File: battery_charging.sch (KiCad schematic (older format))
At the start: 4 parts, among them U8 MCP73831-2-OT

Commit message: clear existing annotations from schematic
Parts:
- renumbered C13 to C?, R16 to R?, R15 to R?, U8 to U?
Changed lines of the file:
@@
 VBAT
 $Comp
-L Battery_Management:MCP73831-2-OT U8
+L Battery_Management:MCP73831-2-OT U?
 U 1 1 5C91A071
 P 3200 2000
-F 0 "U8" H 3200 2481 50  0000 C CNN
+F 0 "U?" H 3200 2481 50  0000 C CNN
 F 1 "MCP73831-2-OT" H 3200 2390 50  0000 C CNN
 F 2 "Package_TO_SOT_SMD:SOT-23-5" H 3250 1750 50  0001 L CIN
@@
 	3600 2100 4000 2100
 $Comp
-L Device:R_Small_US R16
+L Device:R_Small_US R?
 U 1 1 5C91CC9C
 P 4000 1900
-F 0 "R16" H 4068 1946 50  0000 L CNN
+F 0 "R?" H 4068 1946 50  0000 L CNN
 F 1 "10k" H 4068 1855 50  0000 L CNN
 F 2 "Resistor_SMD:R_0603_1608Metric_Pad1.05x0.95mm_HandSolder" H 4000 1900 50  0001 C CNN
@@
 Connection ~ 3200 1650
 $Comp
-L Device:R_Small_US R15
+L Device:R_Small_US R?
 U 1 1 5C91D6DA
 P 2750 2300
-F 0 "R15" H 2818 2346 50  0000 L CNN
+F 0 "R?" H 2818 2346 50  0000 L CNN
 F 1 "2k" H 2818 2255 50  0000 L CNN
 F 2 "Resistor_SMD:R_0603_1608Metric_Pad1.05x0.95mm_HandSolder" H 2750 2300 50  0001 C CNN
@@
 	3200 2500 3200 2300
 $Comp
-L Device:C_Small C13
+L Device:C_Small C?
 U 1 1 5C91EAAB
 P 2600 1900
-F 0 "C13" H 2692 1946 50  0000 L CNN
+F 0 "C?" H 2692 1946 50  0000 L CNN
 F 1 "10uF" H 2692 1855 50  0000 L CNN
 F 2 "Capacitor_SMD:C_0603_1608Metric_Pad1.05x0.95mm_HandSolder" H 2600 1900 50  0001 C CNN

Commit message: fix battery status line to be pulled up to 2.8v, not +vbat
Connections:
- net labels added: VDDIO
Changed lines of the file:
@@
 	4000 2100 4100 2100
 Wire Wire Line
-	4000 1800 4000 1650
-Wire Wire Line
-	4000 1650 3200 1650
-Connection ~ 3200 1650
+	4000 1800 4000 1700
 $Comp
 L Device:R_Small_US R?
@@
 	2600 2500 2750 2500
 Connection ~ 2750 2500
+Text HLabel 4100 1700 2    50   Output ~ 0
+VDDIO
+Wire Wire Line
+	4000 1700 4100 1700
 $EndSCHEMATC

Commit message: upgrade charge circuit to use tp4056, allowing the battery to charge faster without the charger throttling itself
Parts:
- removed C?: 10uF, Capacitor_SMD:C_0603_1608Metric_Pad1.05x0.95mm_HandSolder, symbol Device:C_Small
- removed R?: 10k, Resistor_SMD:R_0603_1608Metric_Pad1.05x0.95mm_HandSolder, symbol Device:R_Small_US
- removed R?: 2k, Resistor_SMD:R_0603_1608Metric_Pad1.05x0.95mm_HandSolder, symbol Device:R_Small_US
- removed U?: MCP73831-2-OT, Package_TO_SOT_SMD:SOT-23-5, symbol Battery_Management:MCP73831-2-OT
- added C?: 10uF, Capacitor_SMD:C_0603_1608Metric_Pad1.05x0.95mm_HandSolder, symbol Device:C_Small
- added R? (x2): 10k, Resistor_SMD:R_0603_1608Metric_Pad1.05x0.95mm_HandSolder, symbol Device:R_Small_US
- added R?: 1.2k, Resistor_SMD:R_0603_1608Metric_Pad1.05x0.95mm_HandSolder, symbol Device:R_Small_US
- added R?: 0.4, Resistor_SMD:R_0603_1608Metric_Pad1.05x0.95mm_HandSolder, symbol Device:R_Small_US
- added U?: TP4056, Package_SO:SOIC-8-1EP_3.9x4.9mm_P1.27mm_EP2.41x3.3mm_ThermalVias, symbol phone:TP4056
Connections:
- net labels added: ~CHRG, ~STDBY
- net labels removed: STAT
- wire segments 18 -> 31
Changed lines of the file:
@@
 Comment4 ""
 $EndDescr
-Text HLabel 4100 2100 2    50   Output ~ 0
-STAT
-Text HLabel 2500 1650 0    50   Input ~ 0
+$Comp
+L phone:TP4056 U?
+U 1 1 5D29DB22
+P 2900 1850
+F 0 "U?" H 2900 2307 39  0000 C CNN
+F 1 "TP4056" H 2900 2232 39  0000 C CNN
+F 2 "Package_SO:SOIC-8-1EP_3.9x4.9mm_P1.27mm_EP2.41x3.3mm_ThermalVias" H 2900 1850 39  0001 C CNN
+F 3 "https://datasheet.lcsc.com/szlcsc/Nanjing-Extension-Microelectronics-TP4056_C16581.pdf" H 2900 1850 39  0001 C CNN
+	1    2900 1850
+	1    0    0    -1
+$EndComp
+Text HLabel 1950 1200 1    50   Input ~ 0
 VDD
-Text HLabel 3650 1900 2    50   Output ~ 0
+Text HLabel 3400 1750 2    50   Output ~ 0
 VBAT
+Text HLabel 2900 2350 3    50   Input ~ 0
+GND
 $Comp
-L Battery_Management:MCP73831-2-OT U?
-U 1 1 5C91A071
-P 3200 2000
-F 0 "U?" H 3200 2481 50  0000 C CNN
-F 1 "MCP73831-2-OT" H 3200 2390 50  0000 C CNN
-F 2 "Package_TO_SOT_SMD:SOT-23-5" H 3250 1750 50  0001 L CIN
-F 3 "http://ww1.microchip.com/downloads/en/DeviceDoc/20001984g.pdf" H 3050 1950 50  0001 C CNN
-	1    3200 2000
+L Device:R_Small_US R?
+U 1 1 5D2A0EB0
+P 3750 1700
+F 0 "R?" H 3818 1746 50  0000 L CNN
+F 1 "10k" H 3818 1655 50  0000 L CNN
+F 2 "Resistor_SMD:R_0603_1608Metric_Pad1.05x0.95mm_HandSolder" H 3750 1700 50  0001 C CNN
+F 3 "~" H 3750 1700 50  0001 C CNN
+	1    3750 1700
+	1    0    0    -1
+$EndComp
+$Comp
+L Device:C_Small C?
+U 1 1 5D2A0EC6
+P 1950 1700
+F 0 "C?" H 2042 1746 50  0000 L CNN
+F 1 "10uF" H 2042 1655 50  0000 L CNN
+F 2 "Capacitor_SMD:C_0603_1608Metric_Pad1.05x0.95mm_HandSolder" H 1950 1700 50  0001 C CNN
+F 3 "~" H 1950 1700 50  0001 C CNN
+	1    1950 1700
 	1    0    0    -1
 $EndComp
 Wire Wire Line
-	3600 1900 3650 1900
+	2900 2350 2900 2300
 Wire Wire Line
-	3200 2600 3200 2500
-Text HLabel 3200 2600 3    50   Input ~ 0
-GND
+	2900 1550 2900 1500
 Wire Wire Line
-	3200 1700 3200 1650
+	2900 1500 2300 1500
 Wire Wire Line
-	3200 1650 2600 1650
+	1950 1600 1950 1500
 Wire Wire Line
-	3600 2100 4000 2100
+	2450 1750 2300 1750
+Wire Wire Line
+	2300 1750 2300 1500
+Connection ~ 2300 1500
+Wire Wire Line
+	2300 1500 1950 1500
 $Comp
 L Device:R_Small_US R?
-U 1 1 5C91CC9C
-P 4000 1900
-F 0 "R?" H 4068 1946 50  0000 L CNN
-F 1 "10k" H 4068 1855 50  0000 L CNN
-F 2 "Resistor_SMD:R_0603_1608Metric_Pad1.05x0.95mm_HandSolder" H 4000 1900 50  0001 C CNN
-F 3 "~" H 4000 1900 50  0001 C CNN
-	1    4000 1900
+U 1 1 5D2AB74A
+P 2400 2150
+F 0 "R?" H 2468 2196 50  0000 L CNN
+F 1 "1.2k" H 2468 2105 50  0000 L CNN
+F 2 "Resistor_SMD:R_0603_1608Metric_Pad1.05x0.95mm_HandSolder" H 2400 2150 50  0001 C CNN
+F 3 "~" H 2400 2150 50  0001 C CNN
+	1    2400 2150
 	1    0    0    -1
 $EndComp
 Wire Wire Line
-	4000 2000 4000 2100
-Connection ~ 4000 2100
+	2450 1950 2400 1950
 Wire Wire Line
-	4000 2100 4100 2100
+	2400 1950 2400 2050
 Wire Wire Line
-	4000 1800 4000 1700
+	2400 2250 2400 2300
+Wire Wire Line
+	2400 2300 2900 2300
+Connection ~ 2900 2300
+Wire Wire Line
+	2900 2300 2900 2150
+Wire Wire Line
+	2400 2300 2300 2300
+Wire Wire Line
+	1950 2300 1950 1800
+Connection ~ 2400 2300
+Wire Wire Line
+	3350 1750 3400 1750
+Text HLabel 4000 1500 1    50   Output ~ 0
+VDDIO
+Wire Wire Line
+	3750 1600 3750 1550
+Wire Wire Line
+	3750 1550 4000 1550
+Wire Wire Line
+	4000 1550 4000 1500
 $Comp
 L Device:R_Small_US R?
-U 1 1 5C91D6DA
-P 2750 2300
-F 0 "R?" H 2818 2346 50  0000 L CNN
-F 1 "2k" H 2818 2255 50  0000 L CNN
-F 2 "Resistor_SMD:R_0603_1608Metric_Pad1.05x0.95mm_HandSolder" H 2750 2300 50  0001 C CNN
-F 3 "~" H 2750 2300 50  0001 C CNN
-	1    2750 2300
+U 1 1 5D2B351B
+P 4250 1750
+F 0 "R?" H 4318 1796 50  0000 L CNN
+F 1 "10k" H 4318 1705 50  0000 L CNN
+F 2 "Resistor_SMD:R_0603_1608Metric_Pad1.05x0.95mm_HandSolder" H 4250 1750 50  0001 C CNN
+F 3 "~" H 4250 1750 50  0001 C CNN
+	1    4250 1750
 	1    0    0    -1
 $EndComp
 Wire Wire Line
-	2750 2200 2750 2100
+	4000 1550 4250 1550
 Wire Wire Line
-	2750 2100 2800 2100
+	4250 1550 4250 1650
+Connection ~ 4000 1550
 Wire Wire Line
-	2750 2400 2750 2500
+	3350 1950 4250 1950
 Wire Wire Line
-	2750 2500 3200 2500
-Connection ~ 3200 2500
+	4250 1950 4250 1850
 Wire Wire Line
-	3200 2500 3200 2300
+	3350 1850 3750 1850
+Wire Wire Line
+	3750 1800 3750 1850
+Wire Wire Line
+	2450 1850 2300 1850
+Wire Wire Line
+	2300 1850 2300 2300
+Connection ~ 2300 2300
+Wire Wire Line
+	2300 2300 1950 2300
+Text HLabel 3850 1850 2    50   Output ~ 0
+~STDBY
+Wire Wire Line
+	3750 1850 3850 1850
+Connection ~ 3750 1850
+Text HLabel 4300 1950 2    50   Output ~ 0
+~CHRG
+Wire Wire Line
+	4250 1950 4300 1950
+Connection ~ 4250 1950
 $Comp
-L Device:C_Small C?
-U 1 1 5C91EAAB
-P 2600 1900
-F 0 "C?" H 2692 1946 50  0000 L CNN
-F 1 "10uF" H 2692 1855 50  0000 L CNN
-F 2 "Capacitor_SMD:C_0603_1608Metric_Pad1.05x0.95mm_HandSolder" H 2600 1900 50  0001 C CNN
-F 3 "~" H 2600 1900 50  0001 C CNN
-	1    2600 1900
+L Device:R_Small_US R?
+U 1 1 5D2C86EE
+P 1950 1350
+F 0 "R?" H 2018 1396 50  0000 L CNN
+F 1 "0.4" H 2018 1305 50  0000 L CNN
+F 2 "Resistor_SMD:R_0603_1608Metric_Pad1.05x0.95mm_HandSolder" H 1950 1350 50  0001 C CNN
+F 3 "~" H 1950 1350 50  0001 C CNN
+	1    1950 1350
 	1    0    0    -1
 $EndComp
 Wire Wire Line
-	2600 1800 2600 1650
-Connection ~ 2600 1650
+	1950 1250 1950 1200
 Wire Wire Line
-	2600 1650 2500 1650
-Wire Wire Line
-	2600 2000 2600 2500
-Wire Wire Line
-	2600 2500 2750 2500
-Connection ~ 2750 2500
-Text HLabel 4100 1700 2    50   Output ~ 0
-VDDIO
-Wire Wire Line
-	4000 1700 4100 1700
+	1950 1500 1950 1450
+Connection ~ 1950 1500
 $EndSCHEMATC

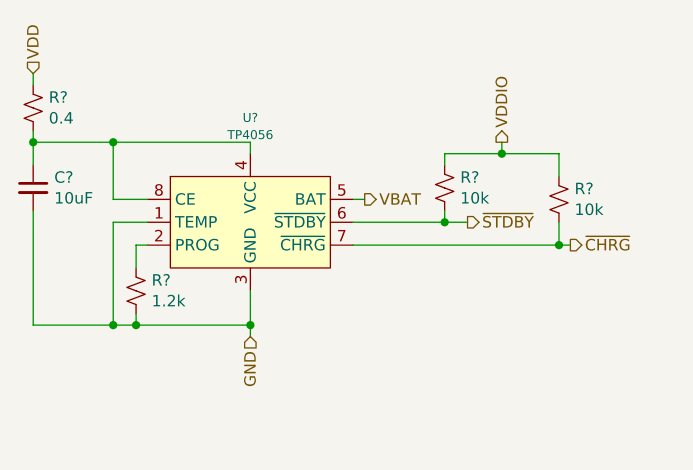
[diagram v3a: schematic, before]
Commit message: annotate schematic and tweak some footprint associations
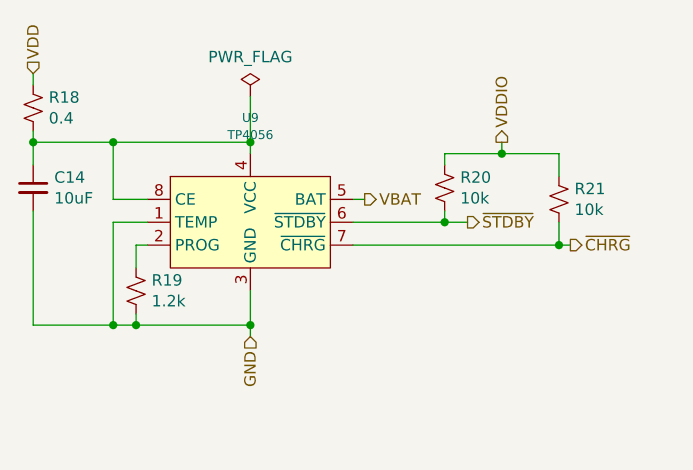
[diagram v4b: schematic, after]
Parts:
- gave numbers to parts that had none: 6
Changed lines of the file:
@@
 $EndDescr
 $Comp
-L phone:TP4056 U?
+L phone:TP4056 U9
 U 1 1 5D29DB22
 P 2900 1850
-F 0 "U?" H 2900 2307 39  0000 C CNN
+F 0 "U9" H 2900 2307 39  0000 C CNN
 F 1 "TP4056" H 2900 2232 39  0000 C CNN
 F 2 "Package_SO:SOIC-8-1EP_3.9x4.9mm_P1.27mm_EP2.41x3.3mm_ThermalVias" H 2900 1850 39  0001 C CNN
@@
 GND
 $Comp
-L Device:R_Small_US R?
+L Device:R_Small_US R20
 U 1 1 5D2A0EB0
 P 3750 1700
-F 0 "R?" H 3818 1746 50  0000 L CNN
+F 0 "R20" H 3818 1746 50  0000 L CNN
 F 1 "10k" H 3818 1655 50  0000 L CNN
 F 2 "Resistor_SMD:R_0603_1608Metric_Pad1.05x0.95mm_HandSolder" H 3750 1700 50  0001 C CNN
@@
 $EndComp
 $Comp
-L Device:C_Small C?
+L Device:C_Small C14
 U 1 1 5D2A0EC6
 P 1950 1700
-F 0 "C?" H 2042 1746 50  0000 L CNN
+F 0 "C14" H 2042 1746 50  0000 L CNN
 F 1 "10uF" H 2042 1655 50  0000 L CNN
 F 2 "Capacitor_SMD:C_0603_1608Metric_Pad1.05x0.95mm_HandSolder" H 1950 1700 50  0001 C CNN
@@
 	2300 1500 1950 1500
 $Comp
-L Device:R_Small_US R?
+L Device:R_Small_US R19
 U 1 1 5D2AB74A
 P 2400 2150
-F 0 "R?" H 2468 2196 50  0000 L CNN
+F 0 "R19" H 2468 2196 50  0000 L CNN
 F 1 "1.2k" H 2468 2105 50  0000 L CNN
 F 2 "Resistor_SMD:R_0603_1608Metric_Pad1.05x0.95mm_HandSolder" H 2400 2150 50  0001 C CNN
@@
 	4000 1550 4000 1500
 $Comp
-L Device:R_Small_US R?
+L Device:R_Small_US R21
 U 1 1 5D2B351B
 P 4250 1750
-F 0 "R?" H 4318 1796 50  0000 L CNN
+F 0 "R21" H 4318 1796 50  0000 L CNN
 F 1 "10k" H 4318 1705 50  0000 L CNN
 F 2 "Resistor_SMD:R_0603_1608Metric_Pad1.05x0.95mm_HandSolder" H 4250 1750 50  0001 C CNN
@@
 Connection ~ 4250 1950
 $Comp
-L Device:R_Small_US R?
+L Device:R_Small_US R18
 U 1 1 5D2C86EE
 P 1950 1350
-F 0 "R?" H 2018 1396 50  0000 L CNN
+F 0 "R18" H 2018 1396 50  0000 L CNN
 F 1 "0.4" H 2018 1305 50  0000 L CNN
 F 2 "Resistor_SMD:R_0603_1608Metric_Pad1.05x0.95mm_HandSolder" H 1950 1350 50  0001 C CNN
@@
 	1950 1500 1950 1450
 Connection ~ 1950 1500
+$Comp
+L power:PWR_FLAG #FLG0101
+U 1 1 5DCD8561
+P 2900 1300
+F 0 "#FLG0101" H 2900 1375 50  0001 C CNN
+F 1 "PWR_FLAG" H 2900 1473 50  0000 C CNN
+F 2 "" H 2900 1300 50  0001 C CNN
+F 3 "~" H 2900 1300 50  0001 C CNN
+	1    2900 1300
+	1    0    0    -1
+$EndComp
+Wire Wire Line
+	2900 1500 2900 1300
+Connection ~ 2900 1500
 $EndSCHEMATC

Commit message: battery charger status lines don't need pullups, as they're built-in to i/o expander
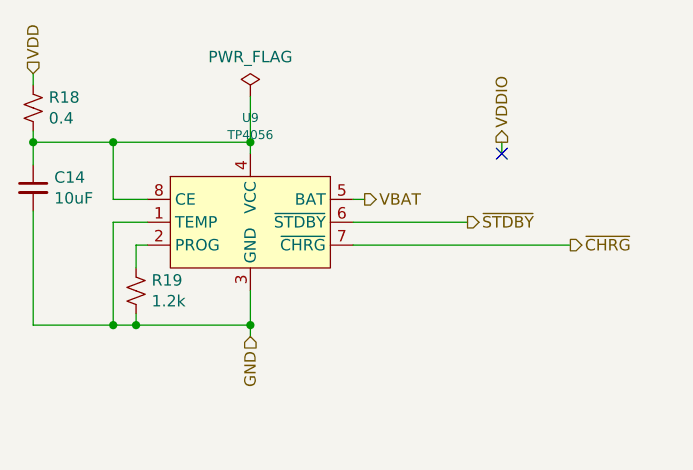
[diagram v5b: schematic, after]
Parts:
- removed R20, R21: 10k, Resistor_SMD:R_0603_1608Metric_Pad1.05x0.95mm_HandSolder, symbol Device:R_Small_US
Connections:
- no-connect marks 0 -> 1
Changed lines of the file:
@@
 GND
-$Comp
-L Device:R_Small_US R20
-U 1 1 5D2A0EB0
-P 3750 1700
-F 0 "R20" H 3818 1746 50  0000 L CNN
-F 1 "10k" H 3818 1655 50  0000 L CNN
-F 2 "Resistor_SMD:R_0603_1608Metric_Pad1.05x0.95mm_HandSolder" H 3750 1700 50  0001 C CNN
-F 3 "~" H 3750 1700 50  0001 C CNN
-	1    3750 1700
-	1    0    0    -1
-$EndComp
 $Comp
 L Device:C_Small C14
@@
 Wire Wire Line
 	3350 1750 3400 1750
-Text HLabel 4000 1500 1    50   Output ~ 0
-VDDIO
-Wire Wire Line
-	3750 1600 3750 1550
-Wire Wire Line
-	3750 1550 4000 1550
-Wire Wire Line
-	4000 1550 4000 1500
-$Comp
-L Device:R_Small_US R21
-U 1 1 5D2B351B
-P 4250 1750
-F 0 "R21" H 4318 1796 50  0000 L CNN
-F 1 "10k" H 4318 1705 50  0000 L CNN
-F 2 "Resistor_SMD:R_0603_1608Metric_Pad1.05x0.95mm_HandSolder" H 4250 1750 50  0001 C CNN
-F 3 "~" H 4250 1750 50  0001 C CNN
-	1    4250 1750
-	1    0    0    -1
-$EndComp
-Wire Wire Line
-	4000 1550 4250 1550
-Wire Wire Line
-	4250 1550 4250 1650
-Connection ~ 4000 1550
-Wire Wire Line
-	3350 1950 4250 1950
-Wire Wire Line
-	4250 1950 4250 1850
-Wire Wire Line
-	3350 1850 3750 1850
-Wire Wire Line
-	3750 1800 3750 1850
 Wire Wire Line
 	2450 1850 2300 1850
@@
 Text HLabel 3850 1850 2    50   Output ~ 0
 ~STDBY
-Wire Wire Line
-	3750 1850 3850 1850
-Connection ~ 3750 1850
 Text HLabel 4300 1950 2    50   Output ~ 0
 ~CHRG
-Wire Wire Line
-	4250 1950 4300 1950
-Connection ~ 4250 1950
 $Comp
 L Device:R_Small_US R18
@@
 	2900 1500 2900 1300
 Connection ~ 2900 1500
+Wire Wire Line
+	4000 1550 4000 1500
+Text HLabel 4000 1500 1    50   Output ~ 0
+VDDIO
+Wire Wire Line
+	3350 1950 4300 1950
+Wire Wire Line
+	3350 1850 3850 1850
+NoConn ~ 4000 1550
 $EndSCHEMATC
